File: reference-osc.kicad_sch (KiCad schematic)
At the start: 3 parts, among them J1 6.5V_POWER_IN

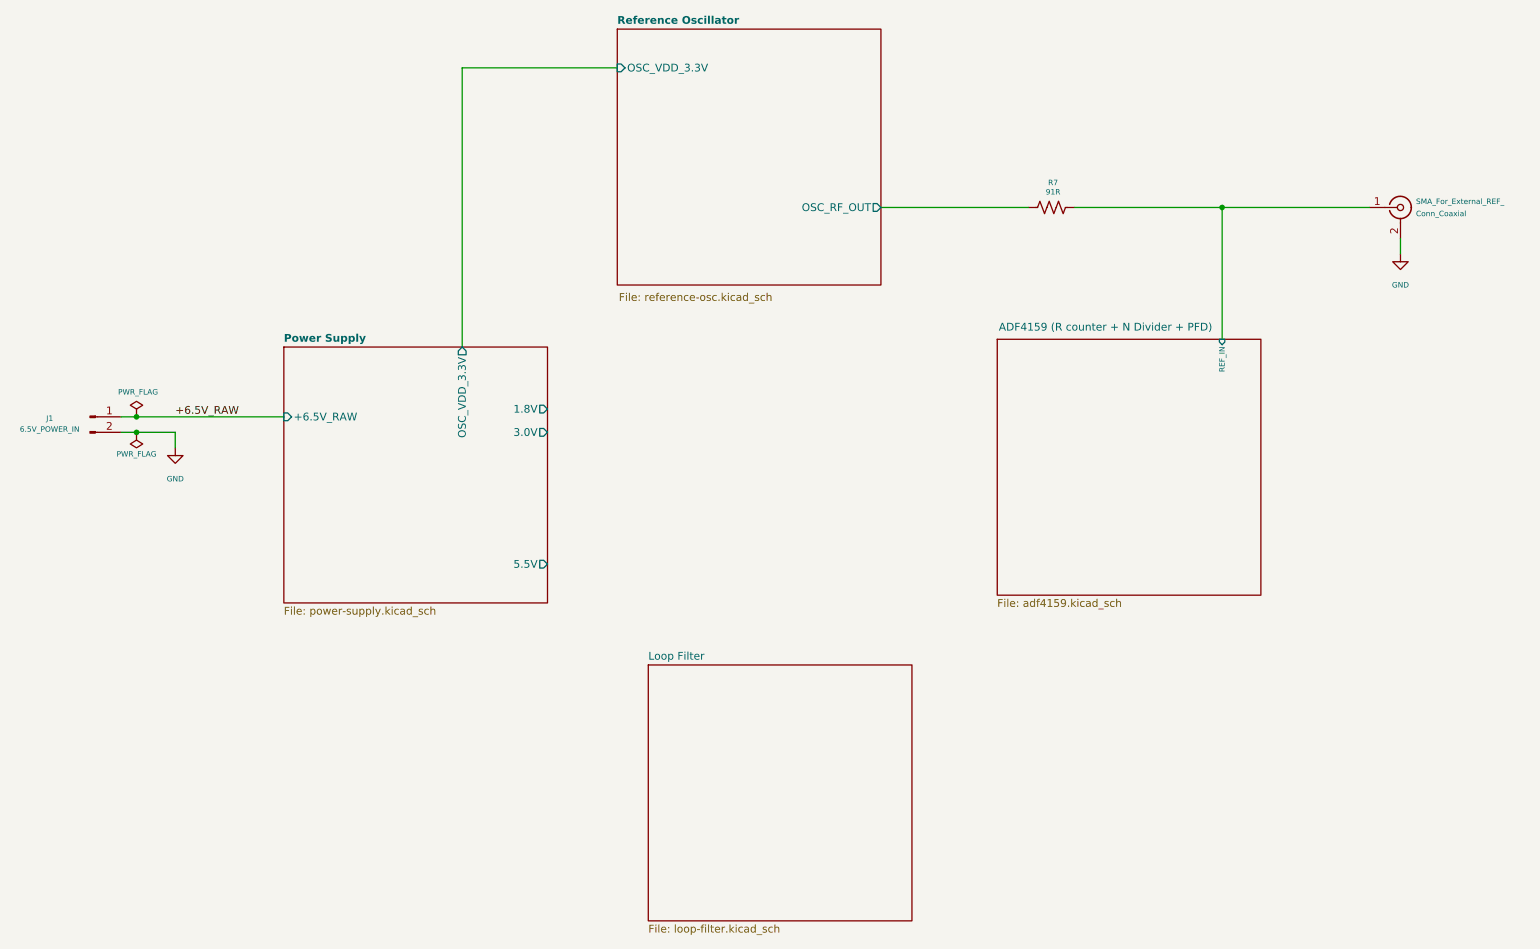
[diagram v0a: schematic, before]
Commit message: Add hierarchical sheets for refosc, loop filter, adf4159. Finish power supply schematic
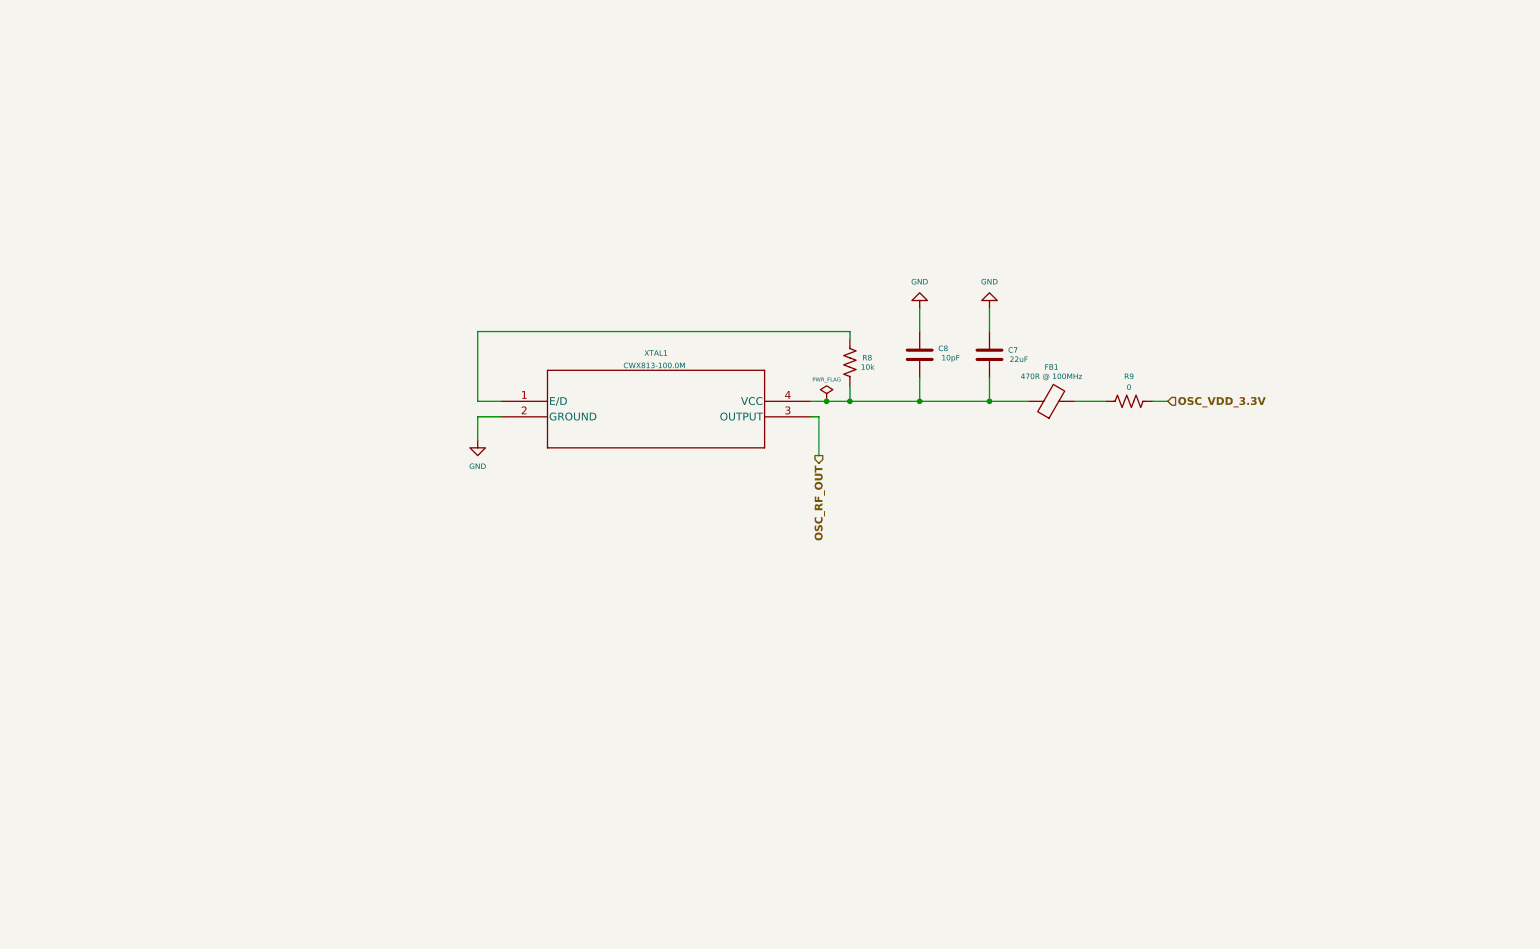
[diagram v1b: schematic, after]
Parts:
- removed J1: 6.5V_POWER_IN, Connector_PinHeader_2.54mm:PinHeader_1x02_P2.54mm_Vertical, symbol Connector:Conn_01x02_Pin
- removed R7: 91R, symbol Device:R_US
- removed SMA_For_External_REF_: Conn_Coaxial, CWX813-100.0M_CNW, symbol Connector:Conn_Coaxial
- added C7: 22uF, Package_TO_SOT_SMD:SOT-23-6, symbol Device:C
- added C8: 10pF, Package_TO_SOT_SMD:SOT-23-6, symbol Device:C
- added FB1: 470R @ 100MHz, Inductor_SMD:L_0603_1608Metric, symbol Device:FerriteBead
- added R8: 10k, symbol Device:R_US
- added R9: 0, symbol Device:R_US
- added XTAL1: CWX813-100.0M, CWX813_crystal_osc_100MHz:CWX813-100.0M_CNW-M, symbol CWX813_crystal_osc_100MHz:CWX813-100.0M
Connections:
- net GND: now also C7.1, C8.1, XTAL1.2 (GROUND)
- new net: R8.1, XTAL1.1 (E/D)
- new net: C7.2, C8.2, FB1.1, R8.2, XTAL1.4 (VCC)
- new net: FB1.2, R9.1
- new net OSC_RF_OUT: XTAL1.3 (OUTPUT)
- new net OSC_VDD_3.3V: R9.2
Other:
- removed sheet ADF4159 (R counter + N Divider + PFD)
- removed sheet Loop Filter
- removed sheet Power Supply
- removed sheet Reference Oscillator
- title: PCB for phase-locked loop system centered around ADF4159 -> Crystal Oscillator providing Reference RF

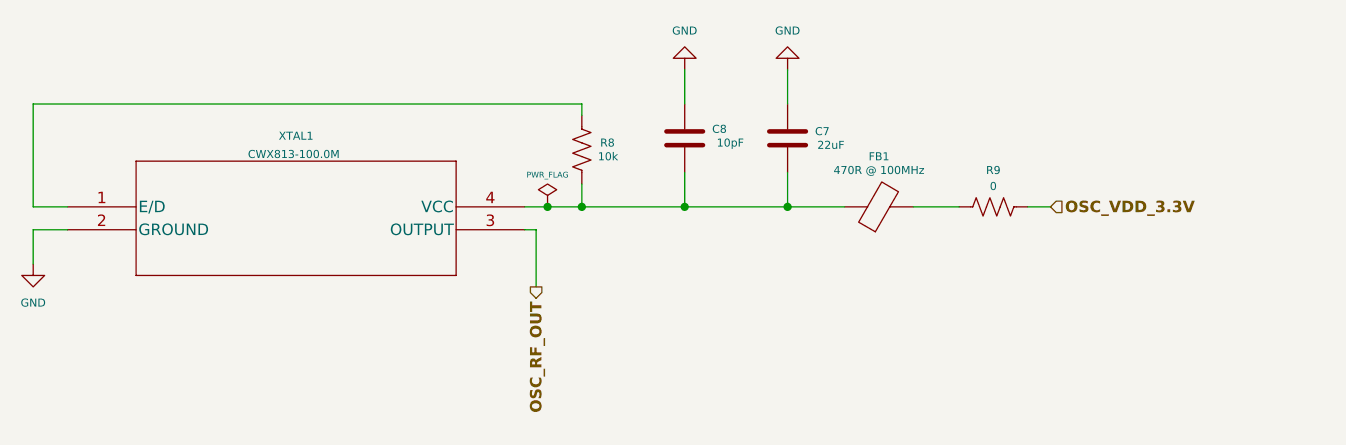
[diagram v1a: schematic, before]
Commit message: Complete Schematic of the PCB
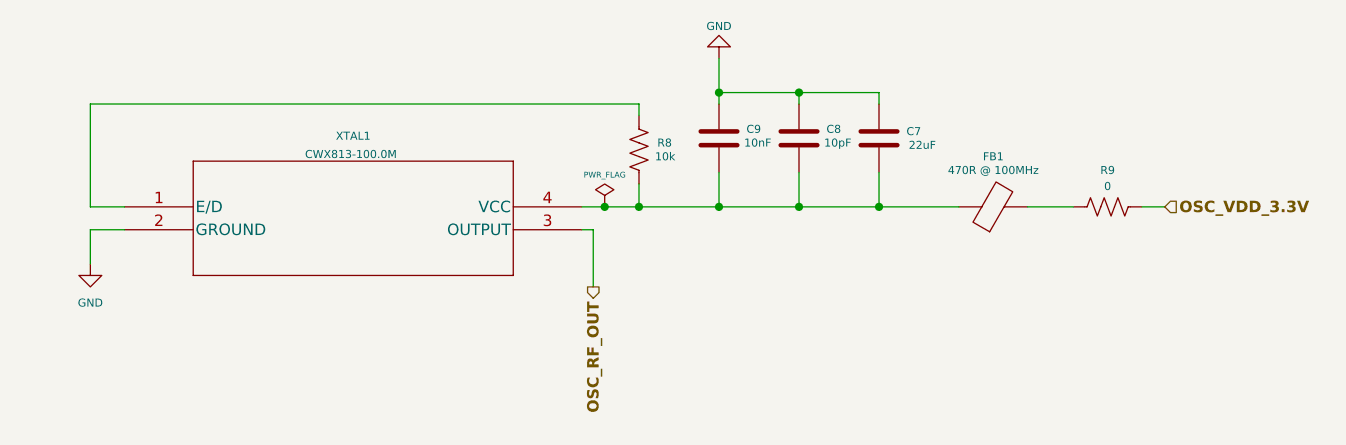
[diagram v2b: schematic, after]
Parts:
- added C9: 10nF, Package_TO_SOT_SMD:SOT-23-6, symbol Device:C
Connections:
- net GND: now also C9.1
- net at C7.2, C8.2, FB1.1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: now also C9.2
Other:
- moved on the sheet: C7, C8, FB1, R8, R9, XTAL1

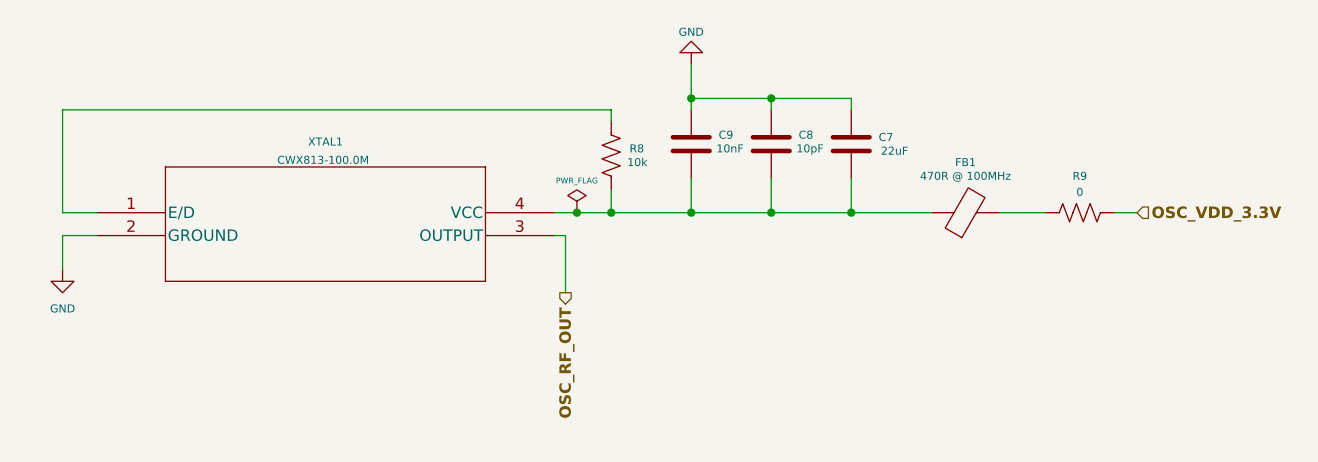
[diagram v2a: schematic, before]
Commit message: Remove 0ohm resistors for EN pins and SMA connector for external REFIN
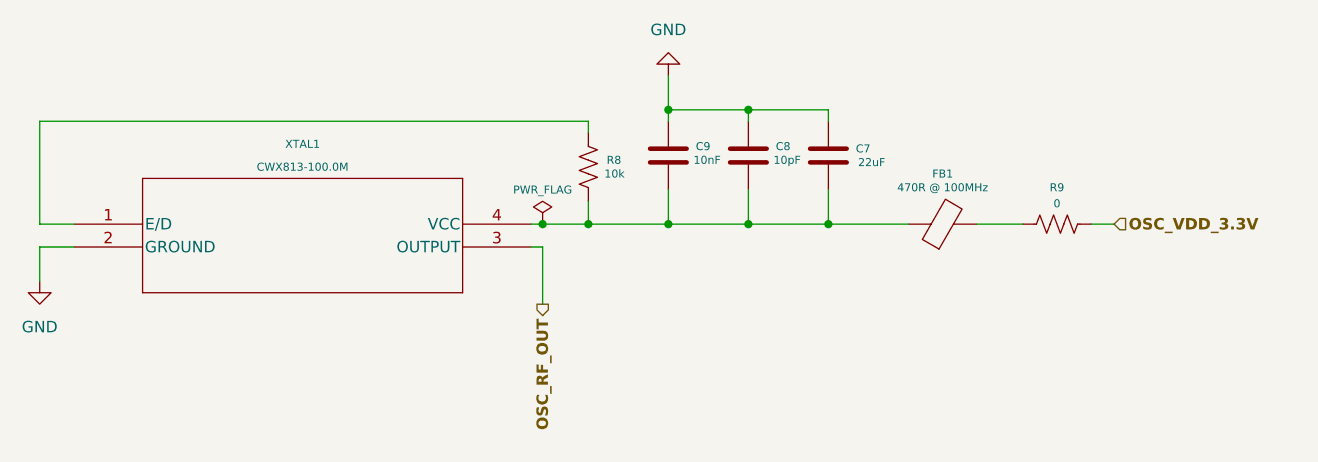
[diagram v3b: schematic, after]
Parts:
- removed XTAL1: CWX813-100.0M, CWX813_crystal_osc_100MHz:CWX813-100.0M_CNW-M, symbol CWX813_crystal_osc_100MHz:CWX813-100.0M
- added XTAL1: CWX813-100.0M, OSC-CWX813:CWX813-100.0M_CNW-L, symbol CWX813-100.0M:CWX813-100.0M
- C7, C8, C9: footprint Package_TO_SOT_SMD:SOT-23-6 -> Capacitor_SMD:C_0402_1005Metric
- R8, R9: footprint (none) -> Capacitor_SMD:C_0402_1005Metric
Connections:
- net GND: now also XTAL1.2 (GROUND)
- net OSC_RF_OUT: now also XTAL1.3 (OUTPUT)
- net at R8.1: now also XTAL1.1 (E/D)
- net at C7.2, C8.2, C9.2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: now also XTAL1.4 (VCC)
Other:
- moved on the sheet: C7, C8, C9, FB1, R8, R9

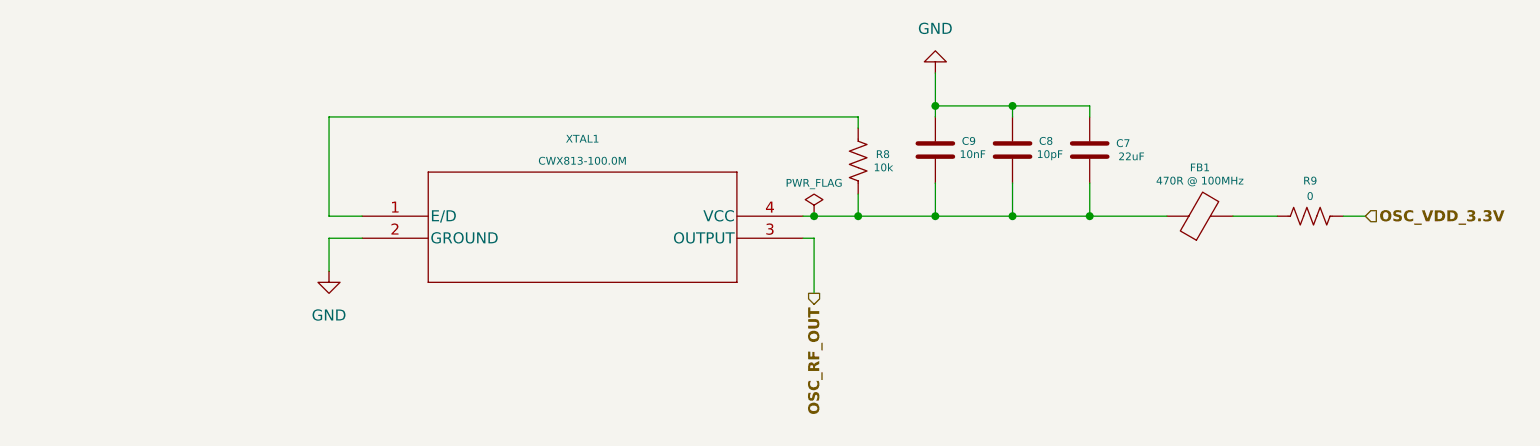
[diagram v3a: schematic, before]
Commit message: Complete and adjust the PCB based on advisor's advice and manufacturer in-stock parts
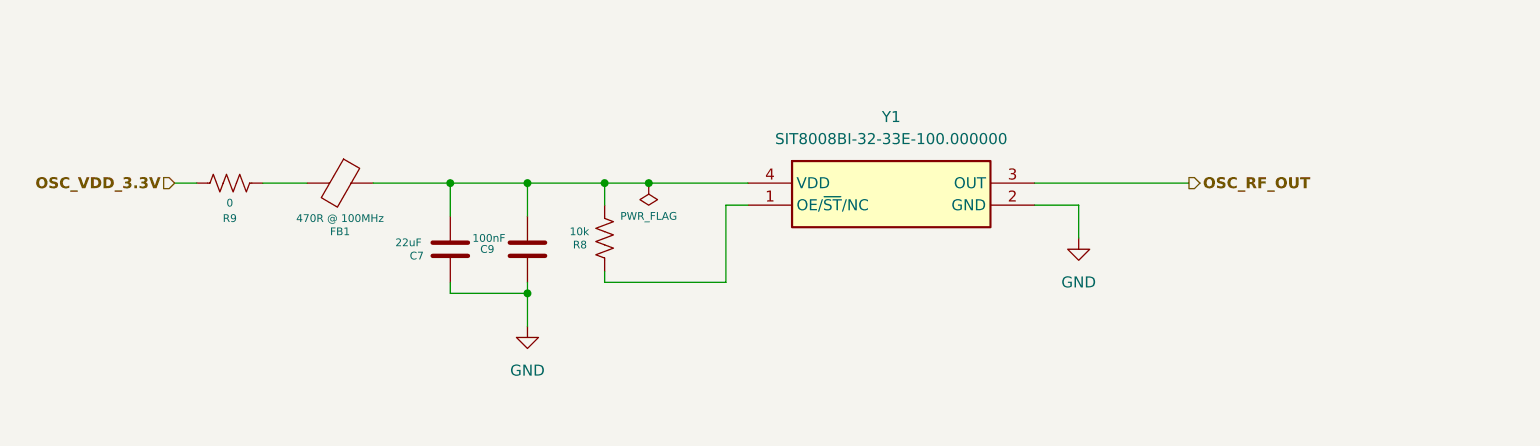
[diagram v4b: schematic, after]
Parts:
- removed C8: 10pF, Capacitor_SMD:C_0402_1005Metric, symbol Device:C
- removed XTAL1: CWX813-100.0M, OSC-CWX813:CWX813-100.0M_CNW-L, symbol CWX813-100.0M:CWX813-100.0M
- added Y1: SIT8008BI-32-33E-100.000000, symbols:SiT8921BM3233N127872000, symbol SIT8008BI-32-33E-100_000000:SIT8008BI-32-33E-100.000000
- C9: value 10nF -> 100nF
- FB1: Current 200mA -> 550mA; DCR Max 0.45R -> 350mΩ max; JLCPCB part: (none) -> C883591; MPN 742792642 -> BLM18AG471SZ1D; Manufacturer Würth Elektronik -> Murata
- R8, R9: footprint Capacitor_SMD:C_0402_1005Metric -> Resistor_SMD:R_0402_1005Metric
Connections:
- net GND: now also Y1.2 (GND)
- net OSC_RF_OUT: now also Y1.3 (OUT)
- net at R8.1: now also Y1.1 (OE/~{ST}/NC)
- net at C7.2, C9.2, FB1.1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: now also Y1.4 (VDD)
